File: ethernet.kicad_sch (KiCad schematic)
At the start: 7 parts

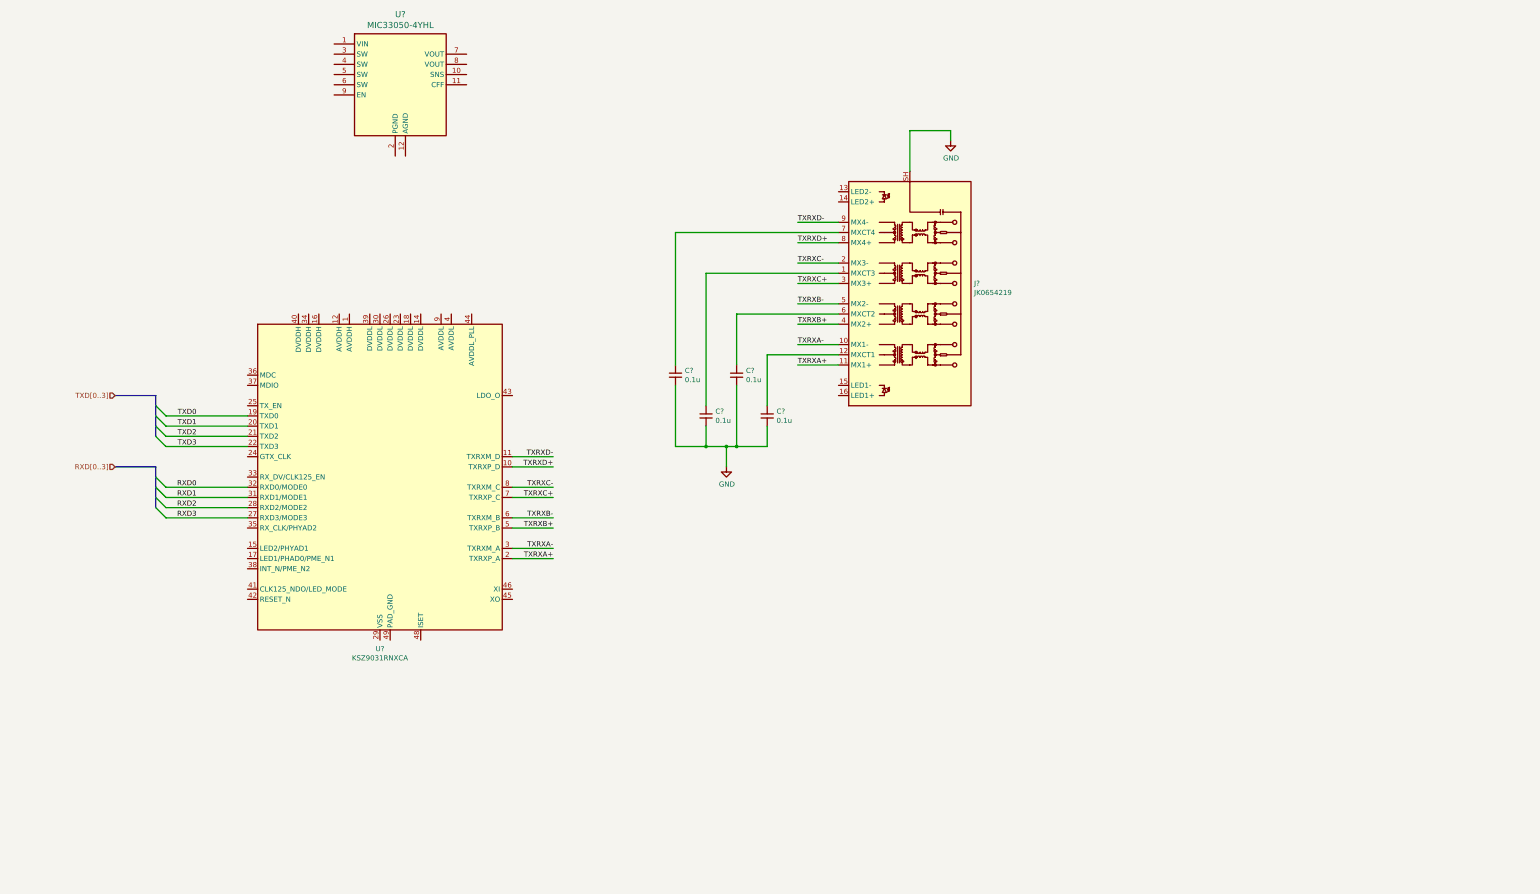
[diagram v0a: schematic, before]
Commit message: WIre Ethernet PHY
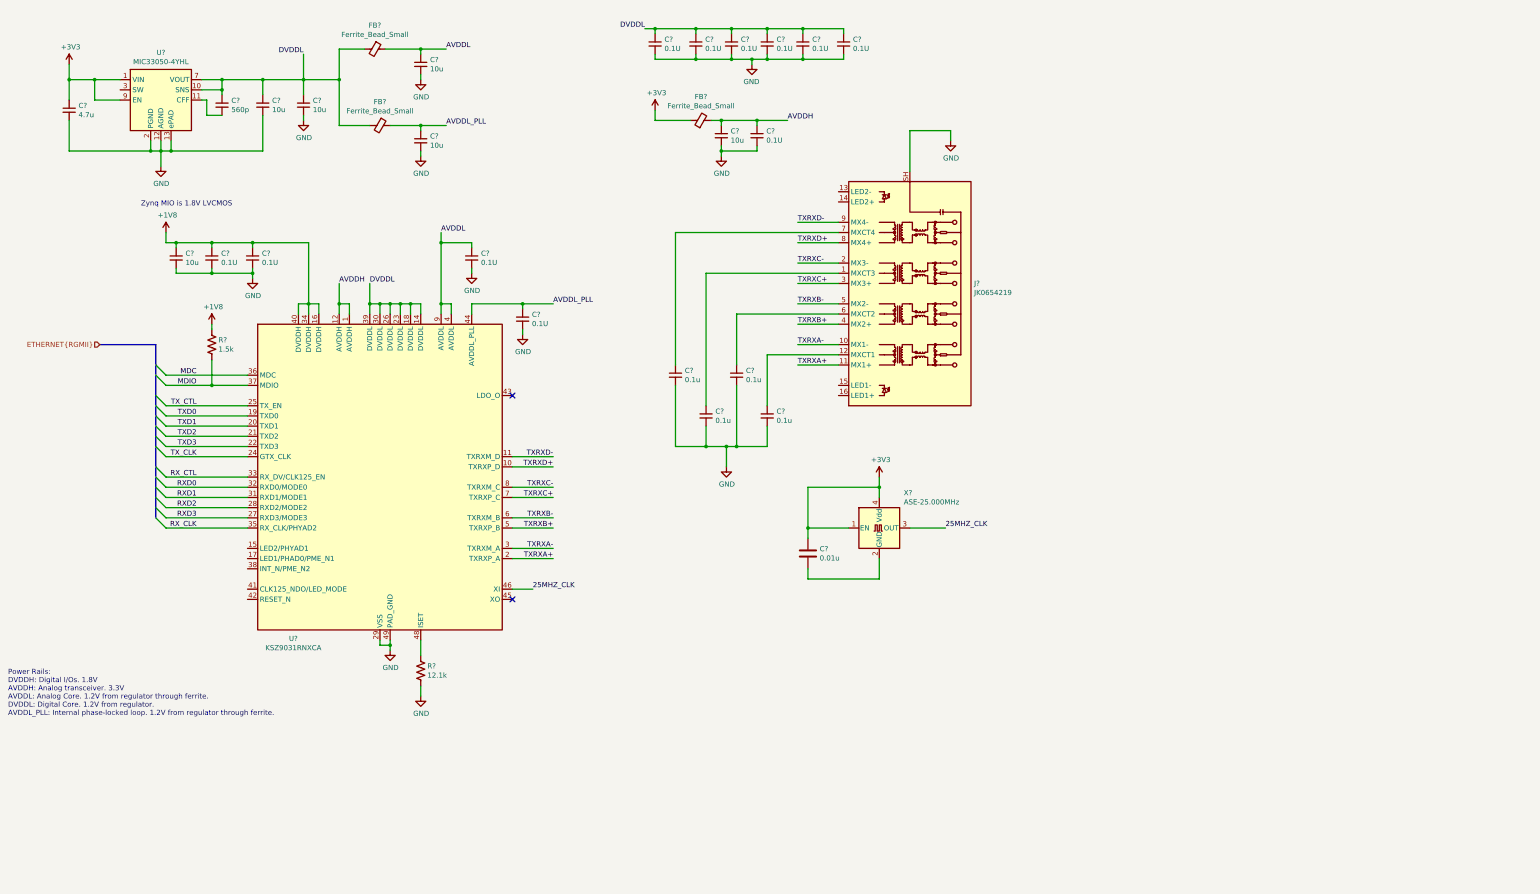
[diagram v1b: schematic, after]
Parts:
- removed U?: MIC33050-4YHL, Package_DFN_QFN:MLF-12-1EP_3x3mm_P0.5mm_EP1.8x1.125mm, symbol Regulator_Switching:MIC33050-4YHL
- added C? (x11): 0.1U, symbol Device:C_Small
- added C? (x6): 10u, symbol Device:C_Small
- added C?: 0.01u, symbol Device:C
- added C?: 4.7u, symbol Device:C_Small
- added C?: 560p, symbol Device:C_Small
- added FB? (x3): Ferrite_Bead_Small, symbol Device:Ferrite_Bead_Small
- added R?: 1.5k, symbol Device:R_US
- added R?: 12.1k, symbol Device:R_US
- added U?: MIC33050-4YHL, Package_DFN_QFN:HDFN-12-1EP_3x3mm_P0.5mm_EP1.8x1.125mm, symbol MIC33050-4YHL:MIC33050-4YHL
- added X?: ASE-25.000MHz, Oscillator:Oscillator_SMD_Abracon_ASE-4Pin_3.2x2.5mm, symbol Oscillator:ASE-xxxMHz
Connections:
- net GND: now also U?.29 (VSS), U?.49 (PAD_GND), C?.2, C?.2, C?.2, C?.2, C?.2, C?.2, C?.2, C?.2, C?.2, C?.2, C?.2, C?.2, C?.2, C?.2, C?.2, C?.2, C?.2, C?.2, R?.2, U?.12 (AGND), U?.13 (ePAD), U?.2 (PGND)
- net AVDDH: now reaches U?.1 (AVDDH)
- net AVDDH: now also U?.12 (AVDDH), C?.1, C?.1, FB?.2
- net DVDDL: now reaches U?.14 (DVDDL)
- net DVDDL: now also U?.18 (DVDDL), U?.23 (DVDDL), U?.26 (DVDDL), U?.30 (DVDDL), U?.39 (DVDDL), C?.1, C?.1, C?.1, C?.1, C?.1, C?.1, C?.1, C?.1, C?.1, FB?.2, FB?.2, U?.10 (SNS), U?.7 (VOUT), U?.8 (VOUT)
- net +1V8: now reaches U?.16 (DVDDH)
- net +1V8: now also U?.34 (DVDDH), U?.40 (DVDDH), C?.1, C?.1, C?.1, R?.1
- net TX_CLK: now reaches U?.24 (GTX_CLK)
- net TX_CTL: now reaches U?.25 (TX_EN)
- net RX_CTL: now reaches U?.33 (RX_DV/CLK125_EN)
- net RX_CLK: now reaches U?.35 (RX_CLK/PHYAD2)
- net MDC: now reaches U?.36 (MDC)
- net MDIO: now reaches U?.37 (MDIO)
- net MDIO: now also R?.2
- net AVDDL: now reaches U?.4 (AVDDL)
- net AVDDL: now also U?.9 (AVDDL), C?.1, C?.1, FB?.1
- net AVDDL_PLL: now reaches U?.44 (AVDDL_PLL)
- net AVDDL_PLL: now also C?.1, C?.1, FB?.1
- net 25MHZ_CLK: now reaches U?.46 (XI)
- net 25MHZ_CLK: now also X?.3 (OUT)
- net at U?.48 (ISET): now also R?.1
- new net: C?.2, X?.2 (GND)
- new net: C?.2, U?.11 (CFF)
- new net: U?.3 (SW), U?.4 (SW), U?.5 (SW), U?.6 (SW)
- new net +3V3: C?.1, C?.1, FB?.1, U?.1 (VIN), U?.9 (EN), X?.1 (EN), X?.4 (Vdd)
- no-connect marks 0 -> 2
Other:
- note added: "Power Rails: DVDDH: Digital I/Os. 1.8V AVDDH: Analog transceiver. 3.3V AVDDL: Analog Core. 1.2V from regulator through ferrite. DVDDL: Digital Core. 1.2V from regulator. AVDDL_PLL: Internal phase-locked loop. 1.2V from regulator through ferrite."
- note added: "Zynq MIO is 1.8V LVCMOS"

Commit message: Finish ethernet sheet, update power calculations
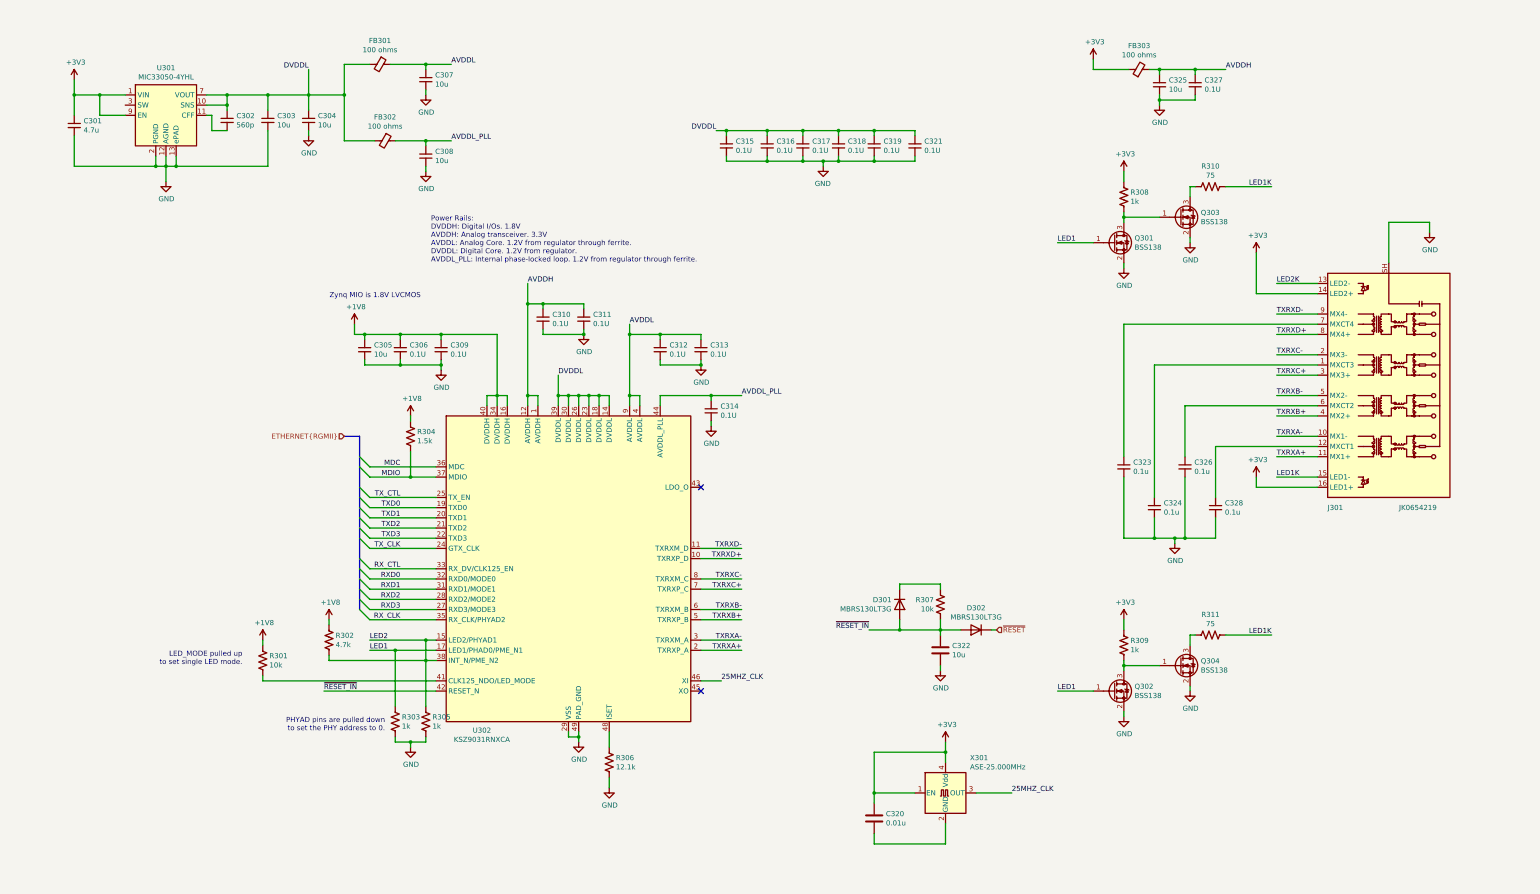
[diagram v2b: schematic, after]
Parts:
- added C310, C311, C313: 0.1U, Capacitor_SMD:C_0402_1005Metric, symbol Device:C_Small
- added C322: 10u, Capacitor_SMD:C_0402_1005Metric, symbol Device:C
- added D301, D302: MBRS130LT3G, Diode_SMD:D_SMB, symbol Device:D
- added Q301, Q302, Q303, Q304: BSS138, Package_TO_SOT_SMD:SOT-23, symbol Transistor_FET:BSS138
- added R301: 10k, symbol Device:R_US
- added R302: 4.7k, symbol Device:R_US
- added R303, R305, R308, R309: 1k, symbol Device:R_US
- added R307: 10k, Resistor_SMD:R_0402_1005Metric, symbol Device:R_US
- added R310, R311: 75, symbol Device:R_US
- C301, C302, C303, C304, C305, C306, C307, C308, C309, C312, C314, C315, C316, C317, C318, C319, C320, C321, C323, C324, C325, C326, C327, C328: renamed from C?; footprint (none) -> Capacitor_SMD:C_0402_1005Metric
- FB301, FB302, FB303: renamed from FB?; value Ferrite_Bead_Small -> 100 ohms; footprint (none) -> Inductor_SMD:L_6.3x6.3_H3
- R304, R306: renamed from R?; footprint (none) -> Resistor_SMD:R_0402_1005Metric
- gave numbers to parts that had none: 4
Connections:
- net +1V8: now also R301.1, R302.1
- net +3V3: now also J301.14 (LED2+), J301.16 (LED1+), R308.1, R309.1
- net AVDDH: now also C310.1, C311.1
- net AVDDL: now also C313.1
- net GND: now also C310.2, C311.2, C313.2, C322.2, Q301.2 (S), Q302.2 (S), Q303.2 (S), Q304.2 (S), R303.2, R305.2
- net LED2: now reaches U302.15 (LED2/PHYAD1)
- net LED2: now also U302.38 (INT_N/PME_N2), R302.2, R305.1
- net LED1: now reaches U302.17 (LED1/PHAD0/PME_N1)
- net LED1: now also Q301.1 (G), Q302.1 (G), R303.1
- net at U302.41 (CLK125_NDO/LED_MODE): now also R301.2
- net ~RESET_IN: now reaches U302.42 (RESET_N)
- net ~RESET_IN: now also C322.1, D301.2 (A), D302.2 (A), R307.2
- net LED2K: now reaches J301.13 (LED2-)
- net LED1K: now reaches J301.15 (LED1-)
- net LED1K: now also R310.2, R311.2
- new net: Q302.3 (D), Q304.1 (G), R309.2
- new net: Q301.3 (D), Q303.1 (G), R308.2
- new net: Q303.3 (D), R310.1
- new net: D301.1 (K), R307.1
- new net: Q304.3 (D), R311.1
- new net ~RESET: D302.1 (K)
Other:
- note added: "LED_MODE pulled up to set single LED mode."
- note added: "PHYAD pins are pulled down to set the PHY address to 0."
- moved on the sheet: C301, C302, C303, C304, C305, C306, C307, C308, C309, C312, C314, C315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
